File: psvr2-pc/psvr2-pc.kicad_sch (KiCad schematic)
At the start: 12 parts, among them J2 USB3_B_Micro, J3 DP_47272, J4 USB_C_Receptacle_USB2.0_14P, P1 USB_C_Plug, Q1 IRLML6244, U1 RP2040, U2 M95256-WMN6P, U3 FUSB302B01MPX, U4 FUSB302B01MPX, Y1 Crystal

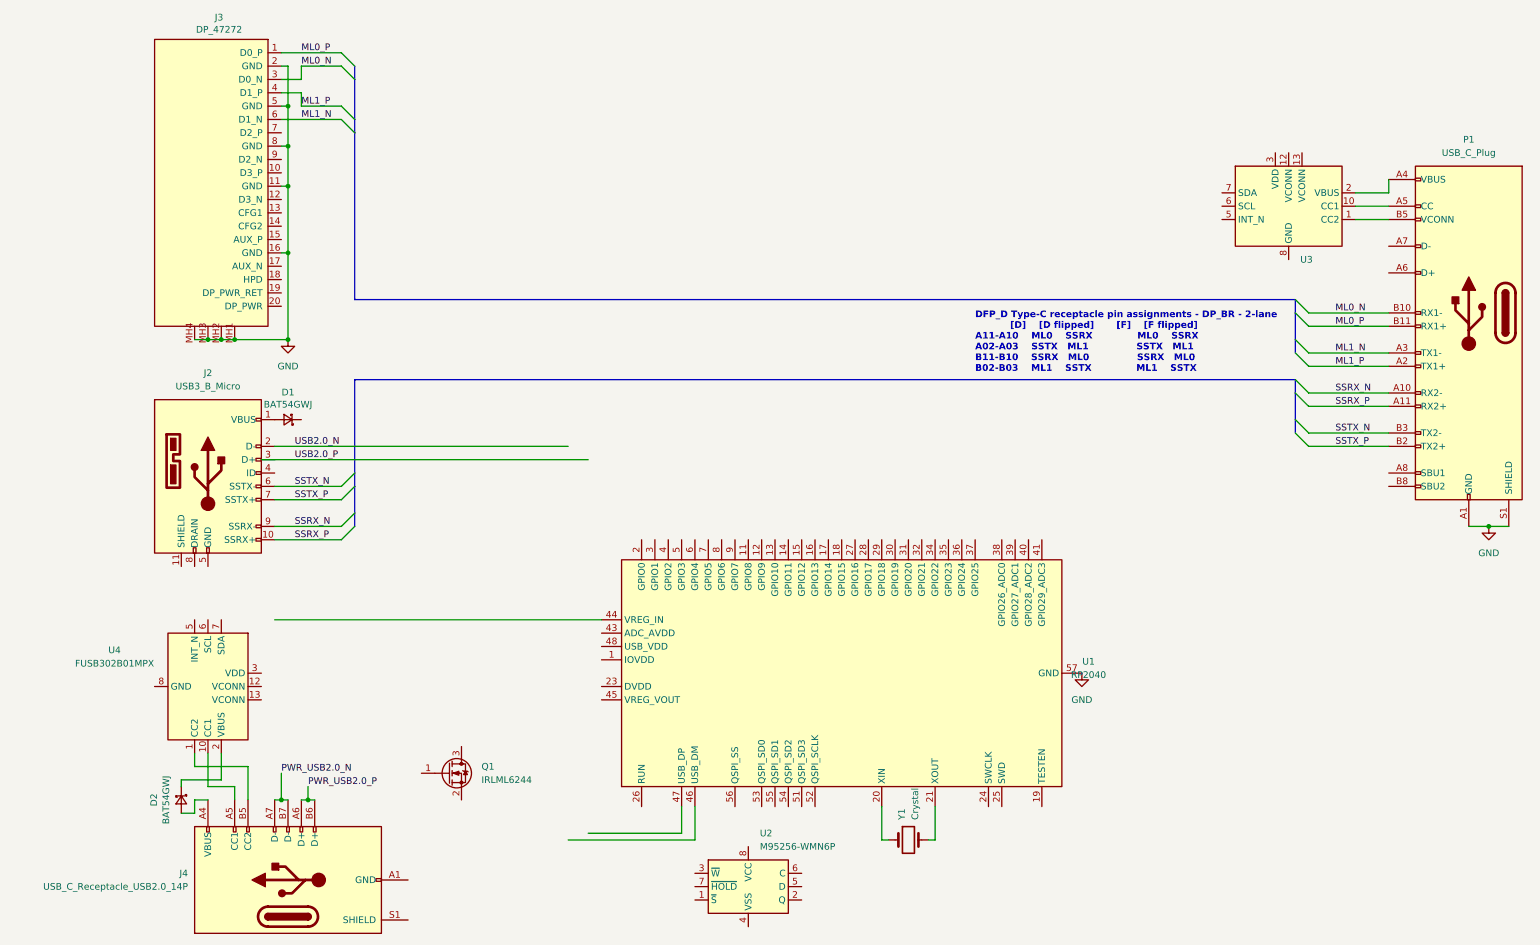
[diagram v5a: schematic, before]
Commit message: Fix the pin assignments to actually make sense and match unflipped D/F.
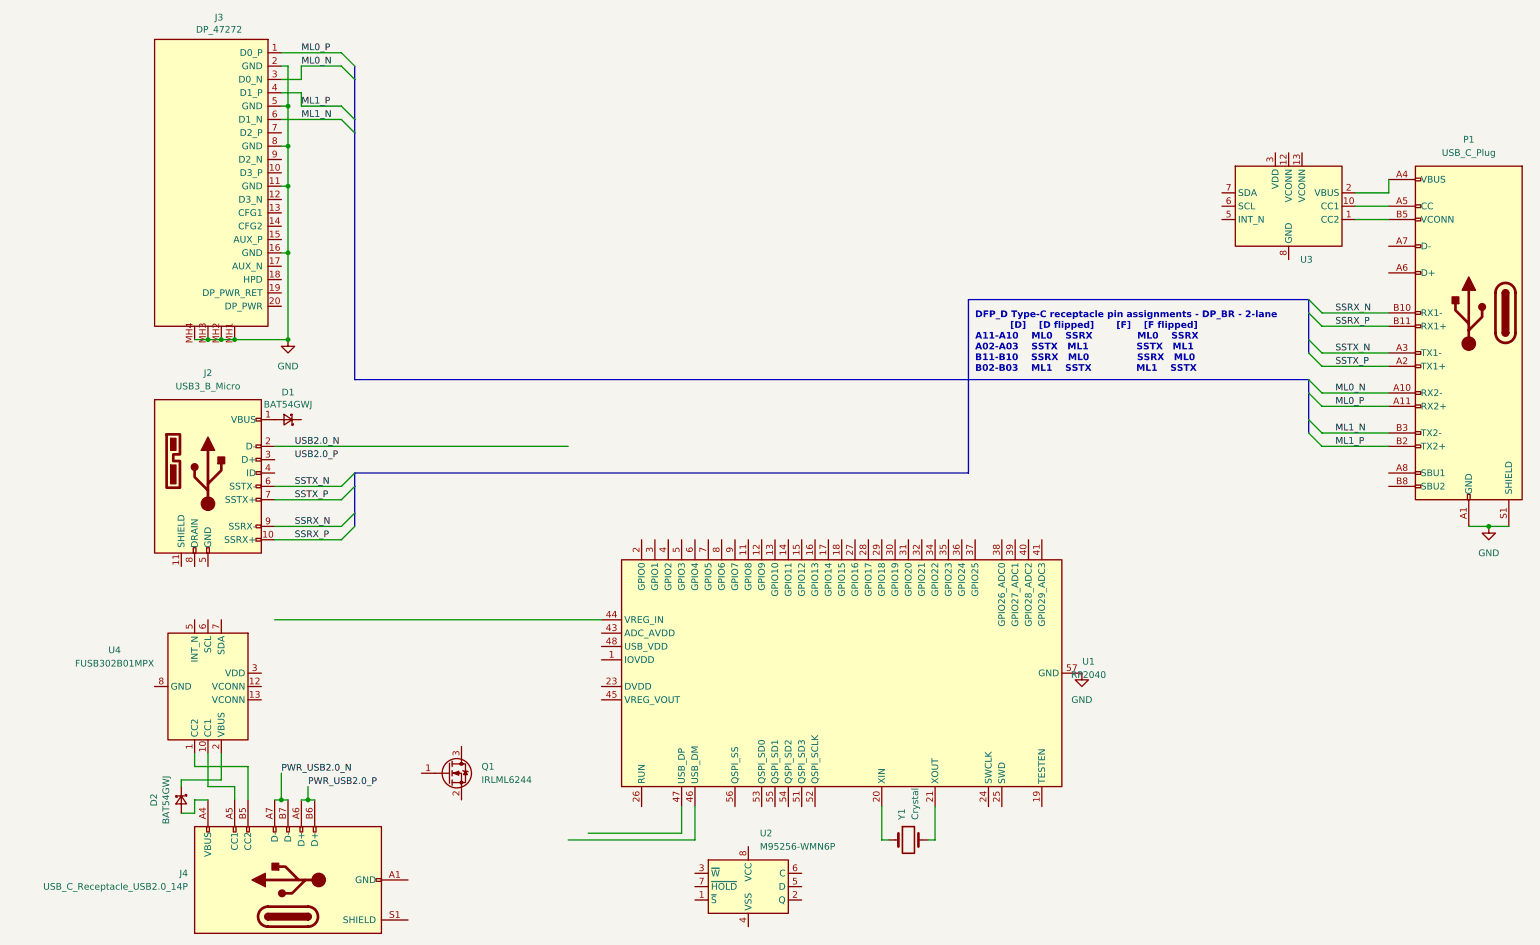
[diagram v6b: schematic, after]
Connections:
- net ML0_N: now also P1.A10 (RX2-); no longer P1.B10 (RX1-)
- net ML0_P: now also P1.A11 (RX2+); no longer P1.B11 (RX1+)
- net ML1_N: now also P1.B3 (TX2-); no longer P1.A3 (TX1-)
- net ML1_P: now also P1.B2 (TX2+); no longer P1.A2 (TX1+)
- net SSRX_N: now also P1.B10 (RX1-); no longer P1.A10 (RX2-)
- net SSRX_P: now also P1.B11 (RX1+); no longer P1.A11 (RX2+)
- net SSTX_N: now also P1.A3 (TX1-); no longer P1.B3 (TX2-)
- net SSTX_P: now also P1.A2 (TX1+); no longer P1.B2 (TX2+)
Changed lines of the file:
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@@
   (junction (at 46.99 157.48) (diameter 0) (color 0 0 0 0)
   )
-  (bus_entry (at 234.95 77.47) (size 2.54 2.54)
+  (bus_entry (at 237.49 62.23) (size 2.54 2.54)
     (stroke (width 0) (type default))
   )
@@
     (stroke (width 0) (type default))
   )
-  (bus_entry (at 234.95 72.39) (size 2.54 2.54)
-    (stroke (width 0) (type default))
-  )
-  (bus_entry (at 234.95 80.01) (size 2.54 2.54)
+  (bus_entry (at 237.49 87.63) (size 2.54 2.54)
+    (stroke (width 0) (type default))
+  )
+  (bus_entry (at 237.49 64.77) (size 2.54 2.54)
     (stroke (width 0) (type default))
   )
@@
     (stroke (width 0) (type default))
   )
-  (bus_entry (at 234.95 64.77) (size 2.54 2.54)
+  (bus_entry (at 237.49 80.01) (size 2.54 2.54)
     (stroke (width 0) (type default))
   )
@@
     (stroke (width 0) (type default))
   )
-  (bus_entry (at 234.95 69.85) (size 2.54 2.54)
-    (stroke (width 0) (type default))
-  )
-  (bus_entry (at 234.95 87.63) (size 2.54 2.54)
-    (stroke (width 0) (type default))
-  )
-  (bus_entry (at 234.95 62.23) (size 2.54 2.54)
+  (bus_entry (at 237.49 85.09) (size 2.54 2.54)
+    (stroke (width 0) (type default))
+  )
+  (bus_entry (at 237.49 72.39) (size 2.54 2.54)
+    (stroke (width 0) (type default))
+  )
+  (bus_entry (at 237.49 77.47) (size 2.54 2.54)
     (stroke (width 0) (type default))
   )
@@
     (stroke (width 0) (type default))
   )
-  (bus_entry (at 234.95 85.09) (size 2.54 2.54)
+  (bus_entry (at 237.49 69.85) (size 2.54 2.54)
     (stroke (width 0) (type default))
   )
@@
     (stroke (width 0) (type default))
   )
-  (bus (pts (xy 55.88 30.48) (xy 55.88 62.23))
-    (stroke (width 0) (type default))
-  )
-  (wire (pts (xy 38.1 92.71) (xy 100.33 92.71))
+  (bus (pts (xy 55.88 30.48) (xy 55.88 77.47))
+    (stroke (width 0) (type default))
+  )
+  (wire (pts (xy 240.03 90.17) (xy 252.73 90.17))
     (stroke (width 0) (type default))
   )
@@
     (stroke (width 0) (type default))
   )
-  (wire (pts (xy 237.49 87.63) (xy 252.73 87.63))
-    (stroke (width 0) (type default))
-  )
   (wire (pts (xy 41.91 40.64) (xy 43.18 40.64))
     (stroke (width 0) (type default))
@@
     (stroke (width 0) (type default))
   )
-  (bus (pts (xy 234.95 77.47) (xy 234.95 80.01))
+  (wire (pts (xy 240.03 80.01) (xy 252.73 80.01))
     (stroke (width 0) (type default))
   )
@@
     (stroke (width 0) (type default))
   )
-  (bus (pts (xy 55.88 77.47) (xy 234.95 77.47))
+  (wire (pts (xy 53.34 97.79) (xy 40.64 97.79))
+    (stroke (width 0) (type default))
+  )
+  (bus (pts (xy 172.72 62.23) (xy 237.49 62.23))
     (stroke (width 0) (type default))
   )
@@
     (stroke (width 0) (type default))
   )
-  (bus (pts (xy 234.95 72.39) (xy 234.95 69.85))
+  (wire (pts (xy 240.03 72.39) (xy 252.73 72.39))
+    (stroke (width 0) (type default))
+  )
+  (bus (pts (xy 237.49 87.63) (xy 237.49 85.09))
     (stroke (width 0) (type default))
   )
@@
     (stroke (width 0) (type default))
   )
-  (wire (pts (xy 252.73 74.93) (xy 237.49 74.93))
-    (stroke (width 0) (type default))
-  )
   (wire (pts (xy 43.18 17.78) (xy 43.18 25.4))
     (stroke (width 0) (type default))
@@
     (stroke (width 0) (type default))
   )
+  (bus (pts (xy 55.88 95.25) (xy 55.88 97.79))
+    (stroke (width 0) (type default))
+  )
   (wire (pts (xy 45.72 25.4) (xy 45.72 22.86))
     (stroke (width 0) (type default))
   )
-  (bus (pts (xy 55.88 62.23) (xy 234.95 62.23))
+  (wire (pts (xy 240.03 82.55) (xy 252.73 82.55))
+    (stroke (width 0) (type default))
+  )
+  (bus (pts (xy 55.88 77.47) (xy 237.49 77.47))
     (stroke (width 0) (type default))
   )
@@
     (stroke (width 0) (type default))
   )
-  (wire (pts (xy 237.49 64.77) (xy 252.73 64.77))
-    (stroke (width 0) (type default))
-  )
   (wire (pts (xy 102.87 123.19) (xy 40.64 123.19))
     (stroke (width 0) (type default))
   )
-  (wire (pts (xy 40.64 97.79) (xy 53.34 97.79))
+  (bus (pts (xy 172.72 95.25) (xy 55.88 95.25))
+    (stroke (width 0) (type default))
+  )
+  (bus (pts (xy 237.49 62.23) (xy 237.49 64.77))
     (stroke (width 0) (type default))
   )
@@
     (stroke (width 0) (type default))
   )
-  (bus (pts (xy 55.88 95.25) (xy 55.88 97.79))
-    (stroke (width 0) (type default))
-  )
   (wire (pts (xy 45.72 157.48) (xy 46.99 157.48))
     (stroke (width 0) (type default))
@@
     (stroke (width 0) (type default))
   )
+  (wire (pts (xy 240.03 64.77) (xy 252.73 64.77))
+    (stroke (width 0) (type default))
+  )
   (wire (pts (xy 166.37 165.1) (xy 165.1 165.1))
     (stroke (width 0) (type default))
   )
-  (wire (pts (xy 237.49 80.01) (xy 252.73 80.01))
-    (stroke (width 0) (type default))
-  )
   (wire (pts (xy 246.38 46.99) (xy 252.73 46.99))
     (stroke (width 0) (type default))
@@
     (stroke (width 0) (type default))
   )
-  (wire (pts (xy 237.49 82.55) (xy 252.73 82.55))
-    (stroke (width 0) (type default))
-  )
   (wire (pts (xy 43.18 53.34) (xy 43.18 69.85))
     (stroke (width 0) (type default))
@@
     (stroke (width 0) (type default))
   )
-  (bus (pts (xy 234.95 80.01) (xy 234.95 85.09))
+  (bus (pts (xy 237.49 64.77) (xy 237.49 69.85))
     (stroke (width 0) (type default))
   )
@@
     (stroke (width 0) (type default))
   )
+  (wire (pts (xy 240.03 87.63) (xy 252.73 87.63))
+    (stroke (width 0) (type default))
+  )
   (bus (pts (xy 55.88 17.78) (xy 55.88 20.32))
     (stroke (width 0) (type default))
@@
     (stroke (width 0) (type default))
   )
-  (bus (pts (xy 55.88 77.47) (xy 55.88 95.25))
+  (bus (pts (xy 172.72 62.23) (xy 172.72 95.25))
     (stroke (width 0) (type default))
   )
@@
     (stroke (width 0) (type default))
   )
-  (wire (pts (xy 237.49 67.31) (xy 252.73 67.31))
-    (stroke (width 0) (type default))
-  )
   (wire (pts (xy 43.18 25.4) (xy 43.18 33.02))
     (stroke (width 0) (type default))
@@
     (stroke (width 0) (type default))
   )
-  (bus (pts (xy 234.95 85.09) (xy 234.95 87.63))
-    (stroke (width 0) (type default))
-  )
-  (bus (pts (xy 234.95 64.77) (xy 234.95 62.23))
-    (stroke (width 0) (type default))
-  )
-  (wire (pts (xy 237.49 72.39) (xy 252.73 72.39))
+  (bus (pts (xy 237.49 69.85) (xy 237.49 72.39))
+    (stroke (width 0) (type default))
+  )
+  (bus (pts (xy 237.49 80.01) (xy 237.49 77.47))
     (stroke (width 0) (type default))
   )
@@
     (stroke (width 0) (type default))
   )
+  (wire (pts (xy 240.03 67.31) (xy 252.73 67.31))
+    (stroke (width 0) (type default))
+  )
   (wire (pts (xy 22.86 160.02) (xy 25.4 160.02))
     (stroke (width 0) (type default))
@@
     (stroke (width 0) (type default))
   )
-  (wire (pts (xy 237.49 90.17) (xy 252.73 90.17))
-    (stroke (width 0) (type default))
-  )
-  (bus (pts (xy 234.95 69.85) (xy 234.95 64.77))
+  (bus (pts (xy 237.49 85.09) (xy 237.49 80.01))
     (stroke (width 0) (type default))
   )
@@
   )
   (wire (pts (xy 22.86 153.67) (xy 22.86 154.94))
+    (stroke (width 0) (type default))
+  )
+  (wire (pts (xy 240.03 74.93) (xy 252.73 74.93))
     (stroke (width 0) (type default))
   )
@@
     (effects (font (face "Courier New") (size 1.27 1.27) (thickness 0.254) bold) (justify left bottom))
   )
-  (label "SSRX_N" (at 242.57 80.01 0) (fields_autoplaced)
+  (label "SSRX_N" (at 242.57 64.77 0) (fields_autoplaced)
     (effects (font (size 1.27 1.27)) (justify left bottom))
   )
@@
     (effects (font (size 1.27 1.27)) (justify left bottom))
   )
-  (label "ML0_P" (at 242.57 67.31 0) (fields_autoplaced)
-    (effects (font (size 1.27 1.27)) (justify left bottom))
-  )
-  (label "SSTX_P" (at 242.57 90.17 0) (fields_autoplaced)
+  (label "ML0_P" (at 242.57 82.55 0) (fields_autoplaced)
+    (effects (font (size 1.27 1.27)) (justify left bottom))
+  )
+  (label "SSTX_P" (at 242.57 74.93 0) (fields_autoplaced)
     (effects (font (size 1.27 1.27)) (justify left bottom))
   )
@@
     (effects (font (size 1.27 1.27)) (justify left bottom))
   )
-  (label "ML1_N" (at 242.57 72.39 0) (fields_autoplaced)
+  (label "ML1_N" (at 242.57 87.63 0) (fields_autoplaced)
     (effects (font (size 1.27 1.27)) (justify left bottom))
   )
@@
     (effects (font (size 1.27 1.27)) (justify left bottom))
   )
-  (label "SSRX_P" (at 242.57 82.55 0) (fields_autoplaced)
+  (label "SSRX_P" (at 242.57 67.31 0) (fields_autoplaced)
     (effects (font (size 1.27 1.27)) (justify left bottom))
   )
@@
     (effects (font (size 1.27 1.27)) (justify left bottom))
   )
-  (label "SSTX_N" (at 242.57 87.63 0) (fields_autoplaced)
-    (effects (font (size 1.27 1.27)) (justify left bottom))
-  )
-  (label "ML0_N" (at 242.57 64.77 0) (fields_autoplaced)
-    (effects (font (size 1.27 1.27)) (justify left bottom))
-  )
-  (label "ML1_P" (at 242.57 74.93 0) (fields_autoplaced)
-    (effects (font (size 1.27 1.27)) (justify left bottom))
-  )
+  (label "SSTX_N" (at 242.57 72.39 0) (fields_autoplaced)
+    (effects (font (size 1.27 1.27)) (justify left bottom))
+  )
+  (label "ML0_N" (at 242.57 80.01 0) (fields_autoplaced)
+    (effects (font (size 1.27 1.27)) (justify left bottom))
+  )
+  (label "ML1_P" (at 242.57 90.17 0) (fields_autoplaced)
+    (effects (font (size 1.27 1.27)) (justify left bottom))
+  )
